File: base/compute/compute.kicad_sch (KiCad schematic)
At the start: 26 parts, among them J1 USB_C_Receptacle_USB2.0_16P, J3 Conn_02x20_Counter_Clockwise, U1 MCP1700T-1202ETT, U3 LD1117S33TR_SOT223, U6 MCP1700T-2802E, U7 USBLC6-2SC6

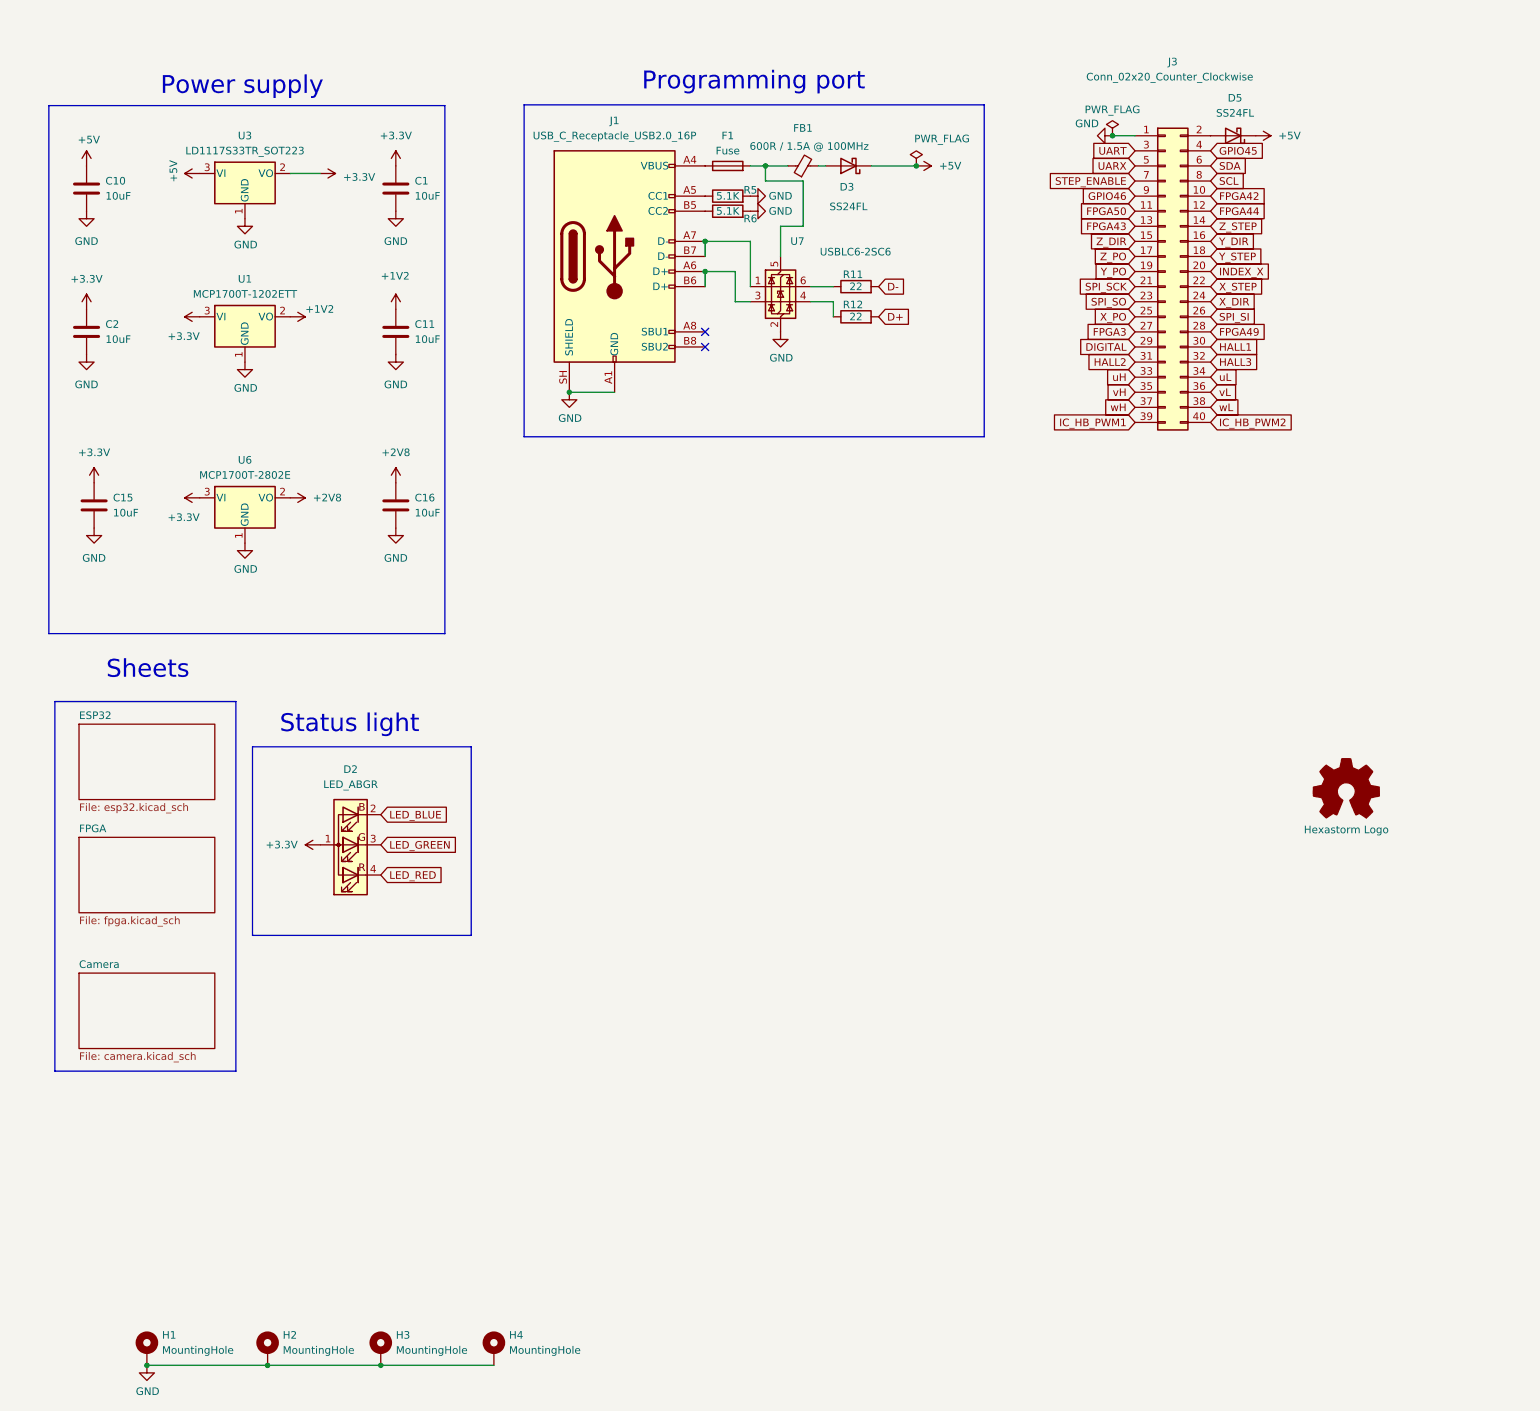
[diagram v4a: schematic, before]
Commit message: quick backup, decided to merge compute and extension
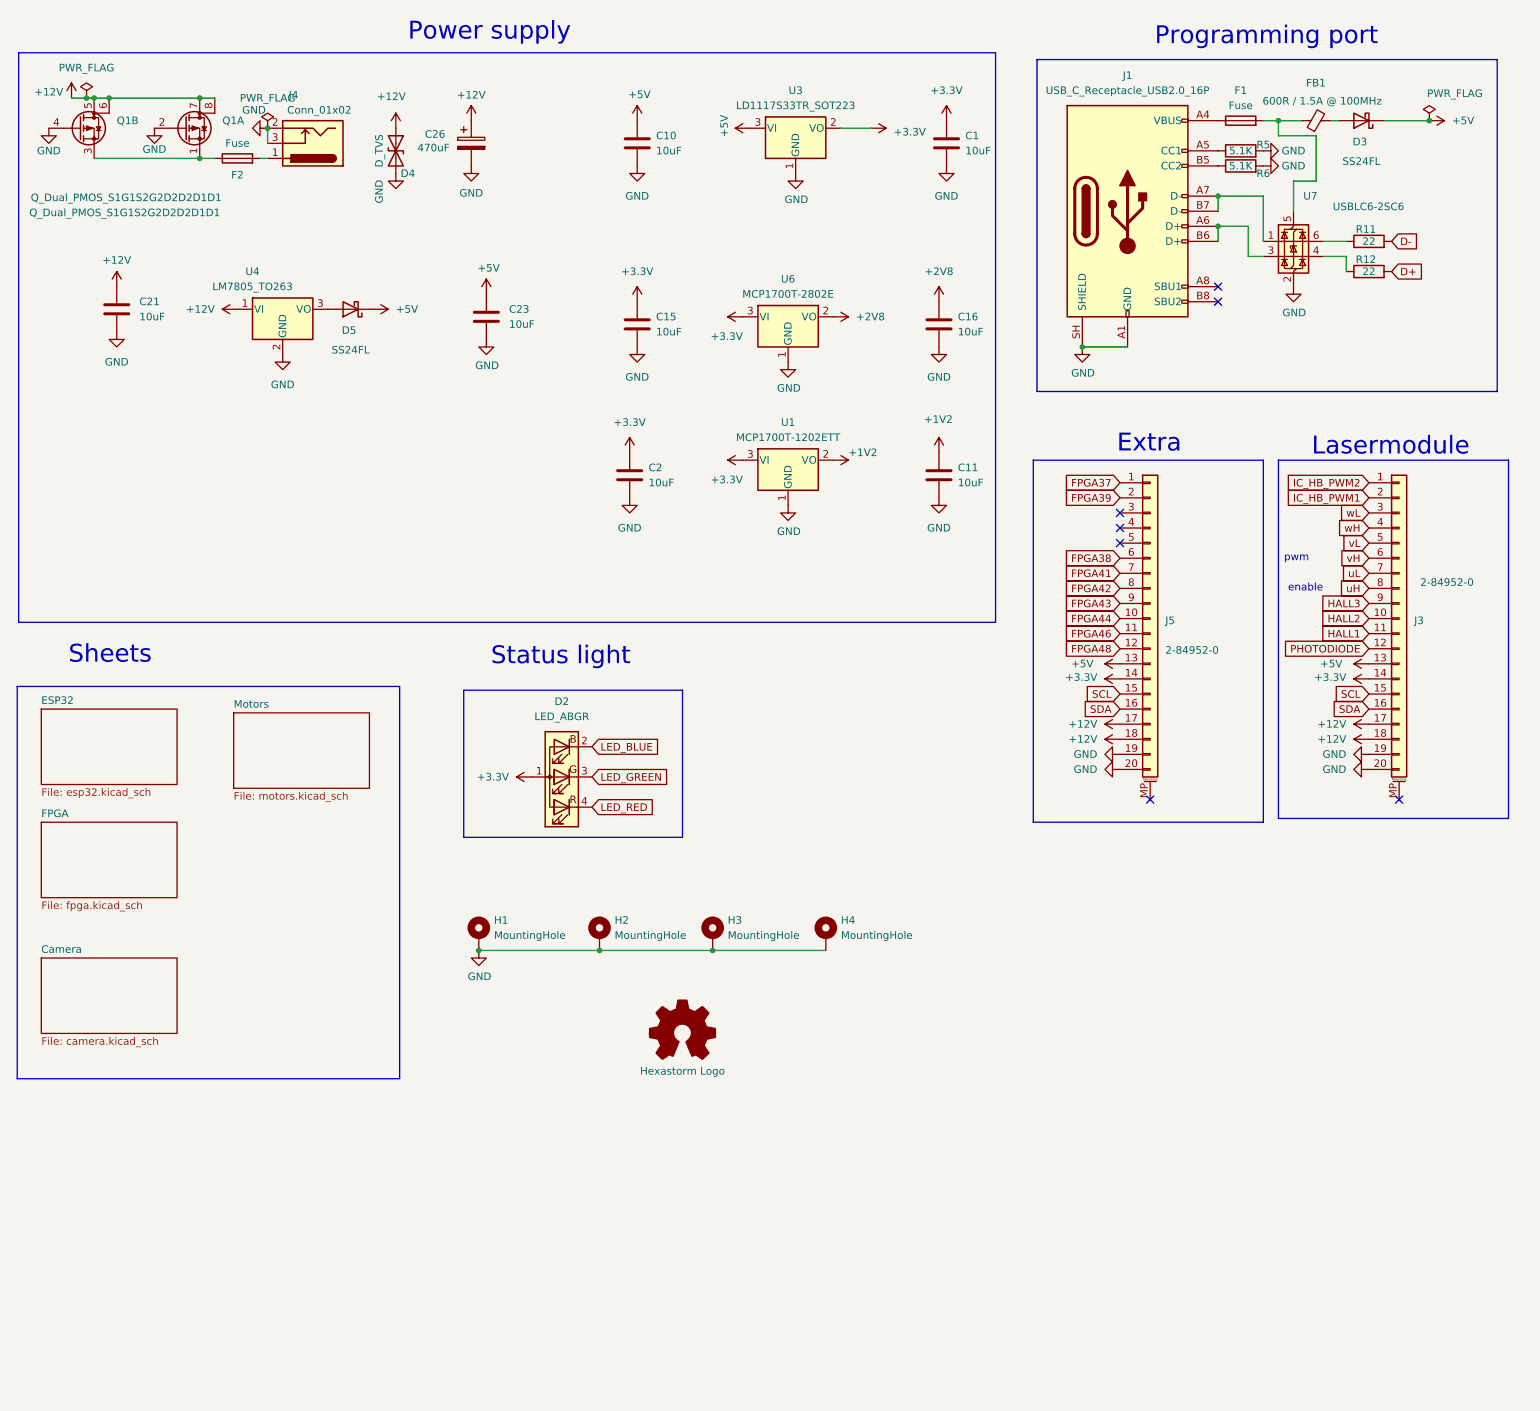
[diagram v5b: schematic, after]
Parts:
- removed J3: Conn_02x20_Counter_Clockwise, Connector_PinHeader_2.54mm:PinHeader_2x20_P2.54mm_Vertical_SMD, symbol Connector_Generic:Conn_02x20_Odd_Even
- added C21, C23: 10uF, Capacitor_SMD:C_0805_2012Metric_Pad1.18x1.45mm_HandSolder, symbol Device:C
- added C26: 470uF, Capacitor_SMD:CP_Elec_10x10.5, symbol Device:C_Polarized
- added D4: D_TVS, Diode_SMD:D_SMB, symbol Device:D_TVS
- added F2: Fuse, footprints:Fuse_2920_7451Metric, symbol Device:Fuse
- added J3, J5: 2-84952-0, footprints:2-84952-0, symbol Connector_Generic_MountingPin:Conn_01x20_MountingPin
- added J4: Conn_01x02, footprints:BarrelJack_CUI_PJ-036AH-SMT_Horizontal, symbol Connector:Barrel_Jack_Switch
- added Q1: Q_Dual_PMOS_S1G1S2G2D2D2D1D1, Package_SO:SOIC-8_3.9x4.9mm_P1.27mm, symbol Transistor_FET:Q_Dual_PMOS_S1G1S2G2D2D2D1D1
- added U4: LM7805_TO263, Package_TO_SOT_SMD:TO-263-3_TabPin2, symbol Regulator_Linear:LM7805_TO220
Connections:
- net +3.3V: now also J3.14 (Pin_14), J5.14 (Pin_14)
- net +5V: now also C23.1, J3.13 (Pin_13), J5.13 (Pin_13)
- net FPGA42: now also J5.8 (Pin_8)
- net FPGA43: now also J5.9 (Pin_9)
- net FPGA44: now also J5.10 (Pin_10)
- net GND: now also C21.2, C23.2, C26.2, D4.2 (A2), J3.19 (Pin_19), J3.20 (Pin_20), J4.2, J4.3, J5.19 (Pin_19), J5.20 (Pin_20), Q1.2 (G), Q1.4 (G), U4.2 (GND)
- net HALL1: now also J3.11 (Pin_11)
- net HALL2: now also J3.10 (Pin_10)
- net HALL3: now also J3.9 (Pin_9)
- net IC_HB_PWM1: now also J3.2 (Pin_2)
- net IC_HB_PWM2: now also J3.1 (Pin_1)
- net SCL: now also J3.15 (Pin_15), J5.15 (Pin_15)
- net SDA: now also J3.16 (Pin_16), J5.16 (Pin_16)
- net uH: now also J3.8 (Pin_8)
- net uL: now also J3.7 (Pin_7)
- net vH: now also J3.6 (Pin_6)
- net vL: now also J3.5 (Pin_5)
- net wH: now also J3.4 (Pin_4)
- net wL: now also J3.3 (Pin_3)
- net at D5.2 (A): now also U4.3 (VO)
- new net: F2.1, Q1.1 (S), Q1.3 (S)
- new net: F2.2, J4.1
- new net +12V: C21.1, C26.1, D4.1 (A1), J3.17 (Pin_17), J3.18 (Pin_18), J5.17 (Pin_17), J5.18 (Pin_18), Q1.5 (D), Q1.6 (D), Q1.7 (D), Q1.8 (D), U4.1 (VI)
- new net FPGA37: J5.1 (Pin_1)
- new net FPGA38: J5.6 (Pin_6)
- new net FPGA39: J5.2 (Pin_2)
- new net FPGA41: J5.7 (Pin_7)
- new net FPGA46: J5.11 (Pin_11)
- new net FPGA48: J5.12 (Pin_12)
- new net PHOTODIODE: J3.12 (Pin_12)
- no-connect marks 2 -> 7
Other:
- added sheet Motors (motors.kicad_sch)
- note added: "Extra"
- note added: "Lasermodule"
- note added: "enable"
- note added: "pwm"
- moved on the sheet: C1, C10, C11, C15, C16, C2, D2, D3, F1, FB1, H1, H2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

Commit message: schema support spindle, fan , 24V, compliant with VEVOR
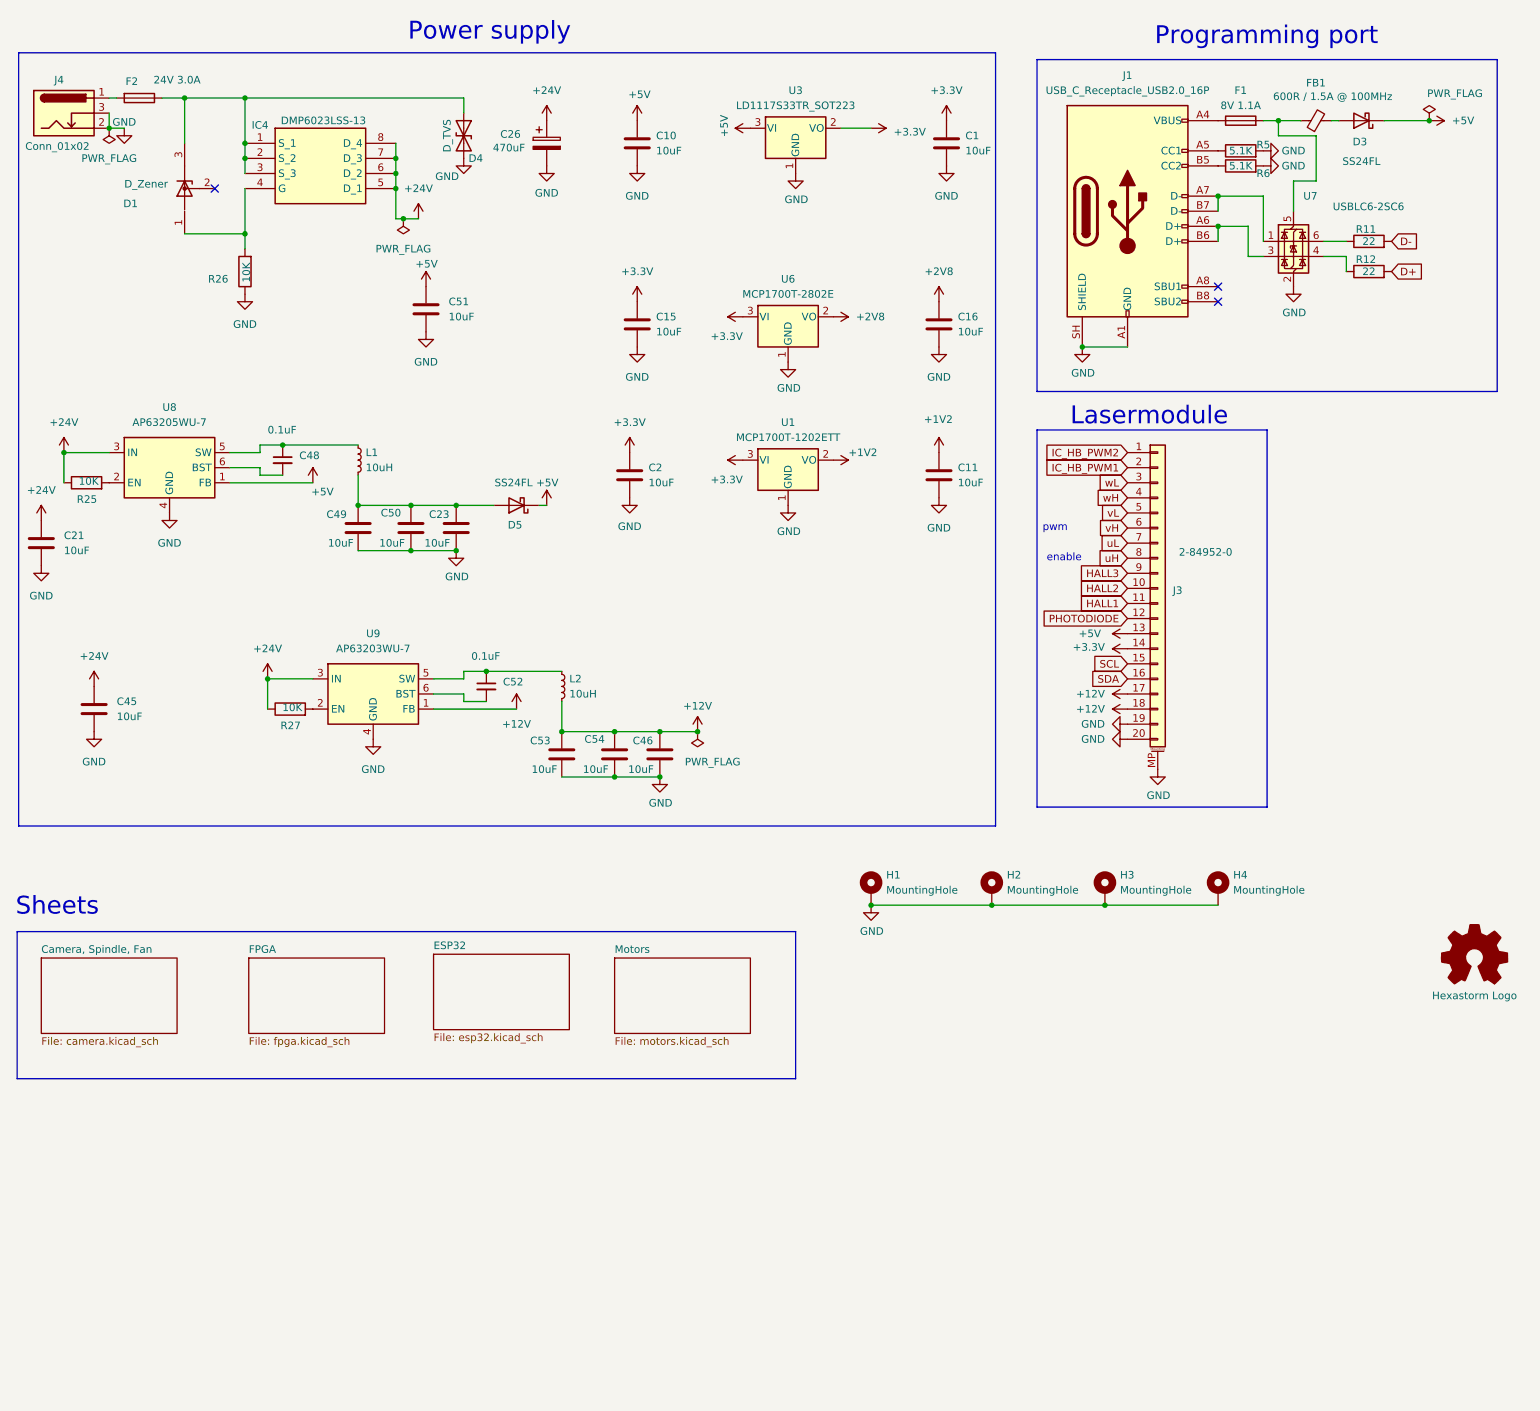
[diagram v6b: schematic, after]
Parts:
- removed D2: LED_ABGR, footprints:LED_Cree-PLCC4_2x2mm_CW, symbol Device:LED_ABGR
- removed J5: 2-84952-0, footprints:2-84952-0, symbol Connector_Generic_MountingPin:Conn_01x20_MountingPin
- removed Q1: Q_Dual_PMOS_S1G1S2G2D2D2D1D1, Package_SO:SOIC-8_3.9x4.9mm_P1.27mm, symbol Transistor_FET:Q_Dual_PMOS_S1G1S2G2D2D2D1D1
- removed U4: LM7805_TO263, Package_TO_SOT_SMD:TO-263-3_TabPin2, symbol Regulator_Linear:LM7805_TO220
- added C45, C46, C49, C50, C51, C53, C54: 10uF, Capacitor_SMD:C_0805_2012Metric_Pad1.18x1.45mm_HandSolder, symbol Device:C
- added C48, C52: 0.1uF, Capacitor_SMD:C_0805_2012Metric_Pad1.18x1.45mm_HandSolder, symbol Device:C_Small
- added D1: D_Zener, Package_TO_SOT_SMD:SOT-23, symbol compute_library:Sot23-zener
- added IC4: DMP6023LSS-13, Package_SO:SOIC-8_3.9x4.9mm_P1.27mm, symbol compute_library:DMP6023LSS-13
- added L1, L2: 10uH, Inductor_SMD:L_Bourns_SRP5030T, symbol Device:L_Small
- added R25, R26, R27: 10K, Resistor_SMD:R_0805_2012Metric, symbol Device:R
- added U8: AP63205WU-7, Package_TO_SOT_SMD:TSOT-23-6, symbol Regulator_Switching:AP63205WU
- added U9: AP63203WU-7, Package_TO_SOT_SMD:TSOT-23-6, symbol Regulator_Switching:AP63205WU
- C1, C10, C11, C15, C16, C2: farnell# 3010126 -> 3790440; manf# CL21A106KAYNNNE -> GRM21BR61H106KE43L; mouser# 187-CL21A106KAYNNNE -> 81-GRM21BR61H106KE3L
- C21, C23: farnell# CL21A106KAYNNNE -> 3790440; manf# 187-CL21A106KAYNNNE -> GRM21BR61H106KE43L; mouser# 3010126 -> 81-GRM21BR61H106KE3L
- C26: farnell# 2326208 -> 2507737; manf# EEE-FK1E471GP -> EEEFK1V471SP; mouser# 667-EEE-FK1E471GP -> 667-EEE-FK1V471SP
- F1: value Fuse -> 8V 1.1A
- F2: value Fuse -> 24V 3.0A
- J3: farnell# 3404513 -> 1245274; manf# 2399744 -> 2-84952-0
- R11, R12: farnell# 2303365 -> 1652962; manf# ERJ-6ENF22R0V -> CRCW080522R0FKEA; mouser# 667-ERJ-6ENF22R0V -> 71-CRCW0805-22-E3
- U7: farnell# (none) -> 1269406; manf# (none) -> USBLC6-2SC6; mouser# (none) -> 511-USBLC6-2SC6
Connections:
- net +12V: now also C46.1, C53.1, C54.1, L2.2, U9.1 (FB); no longer C21.1, C26.1, D4.1 (A1)
- net +5V: now also C51.1, U8.1 (FB); no longer C23.1
- net GND: now also J3.MP (MountPin), C45.2, C46.2, C49.2, C50.2, C51.2, C53.2, C54.2, R26.1, U8.4 (GND), U9.4 (GND)
- net at F2.1: now also D4.1 (A1), D1.3 (K), IC4.1 (S_1), IC4.2 (S_2), IC4.3 (S_3)
- net at D5.2 (A): now also C23.1, C49.1, C50.1, L1.2
- new net: C52.1, L2.1, U9.5 (SW)
- new net: C52.2, U9.6 (BST)
- new net: R27.2, U9.2 (EN)
- new net: C48.1, L1.1, U8.5 (SW)
- new net: C48.2, U8.6 (BST)
- new net: D1.1 (K), IC4.4 (G), R26.2
- new net: R25.2, U8.2 (EN)
- new net +24V: C21.1, C26.1, C45.1, IC4.5 (D_1), IC4.6 (D_2), IC4.7 (D_3), IC4.8 (D_4), R25.1, R27.1, U8.3 (IN), U9.3 (IN)
- no-connect marks 7 -> 3
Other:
- sheet Camera renamed Camera, Spindle, Fan
- note removed: "Extra"
- note removed: "Status light"
- moved on the sheet: C21, C23, C26, D4, D5, F2, H1, H2, H3, H4, J3, J4

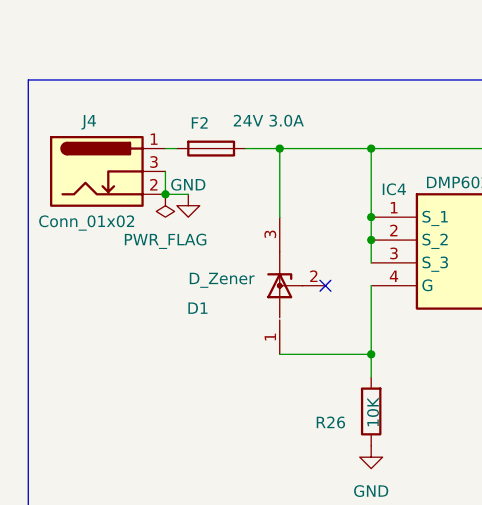
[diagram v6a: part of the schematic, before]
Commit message: board passes all tests
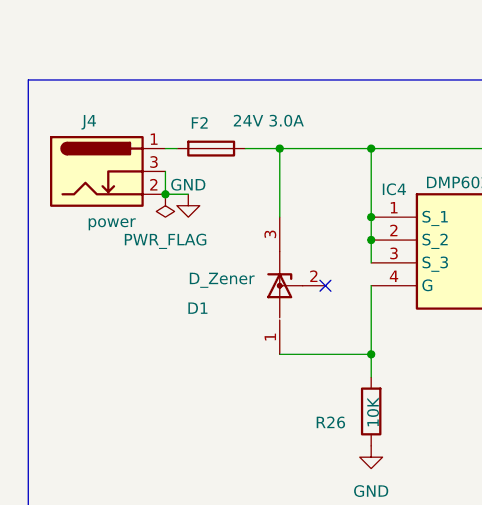
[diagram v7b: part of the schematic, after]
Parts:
- J4: value Conn_01x02 -> power
- L2: mouser# 652-SRP5030T-100M -> 652-SRP5030T-100M
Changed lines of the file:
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@@
 	(title_block
 		(title "Firestarter ")
-		(date "2024-10-26")
+		(date "2026-04-30")
 		(company "Hexastorm")
 		(comment 1 "v1")
@@
 			)
 		)
-		(property "Value" "Conn_01x02"
+		(property "Value" "power"
 			(at 41.148 36.068 0)
 			(show_name no)
@@
 			)
 		)
-		(property "mouser#" "652-SRP5030T-100M "
+		(property "mouser#" "652-SRP5030T-100M"
 			(at 120.65 127 0)
 			(hide yes)
